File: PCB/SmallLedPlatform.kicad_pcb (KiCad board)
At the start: 4 copper layers, 44.7 x 36.1 mm, 47 parts, among them J101 USB_C_Receptacle, J102 Conn_02x05_Odd_Even, J103 Conn_01x03_Male, J104 Conn_01x03_Male, Q101 AO3400A, U101 STM32G0B1CBTx, U102 USBLC6-2P6, U103 TCPP01-M12, U201 TPS5430DDA, U202 XC6206PxxxMR

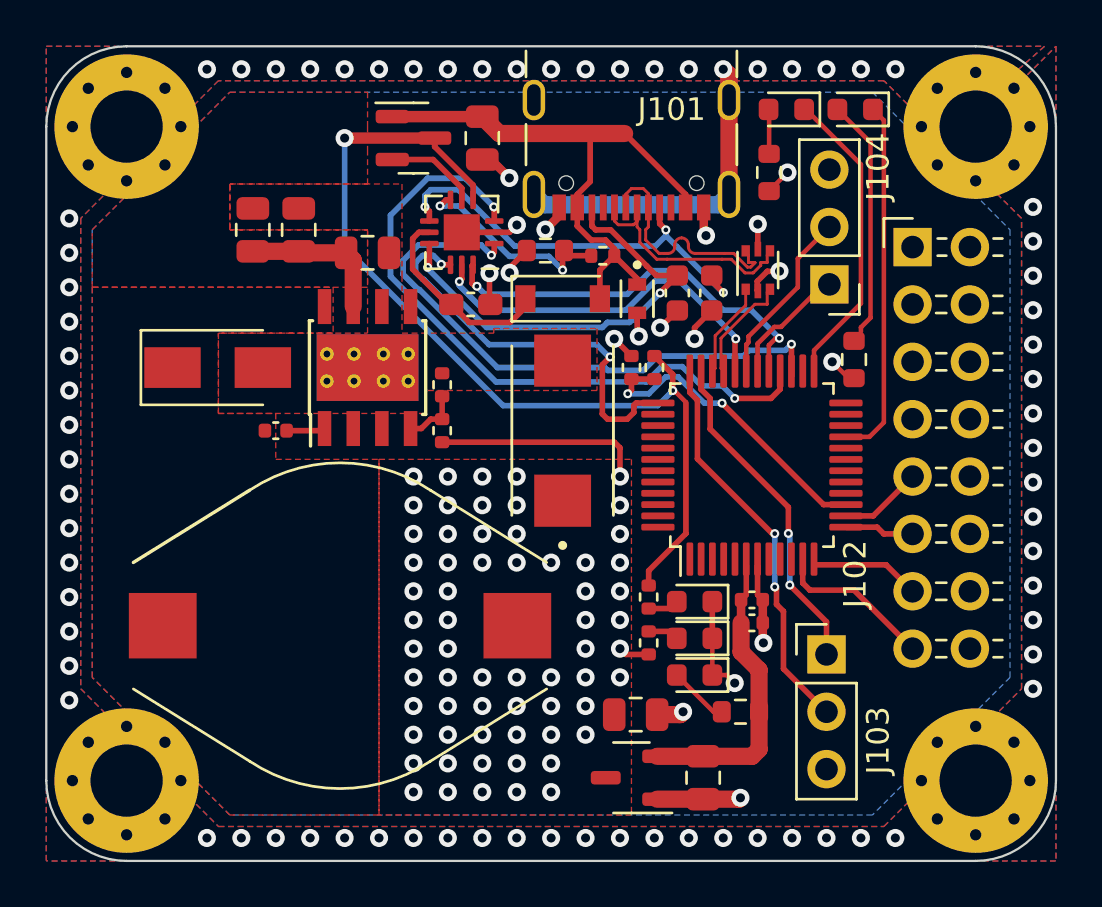
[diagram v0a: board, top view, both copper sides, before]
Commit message: Add a new DC/DC solution to the schematic
Components has been added to layout, but not properly done
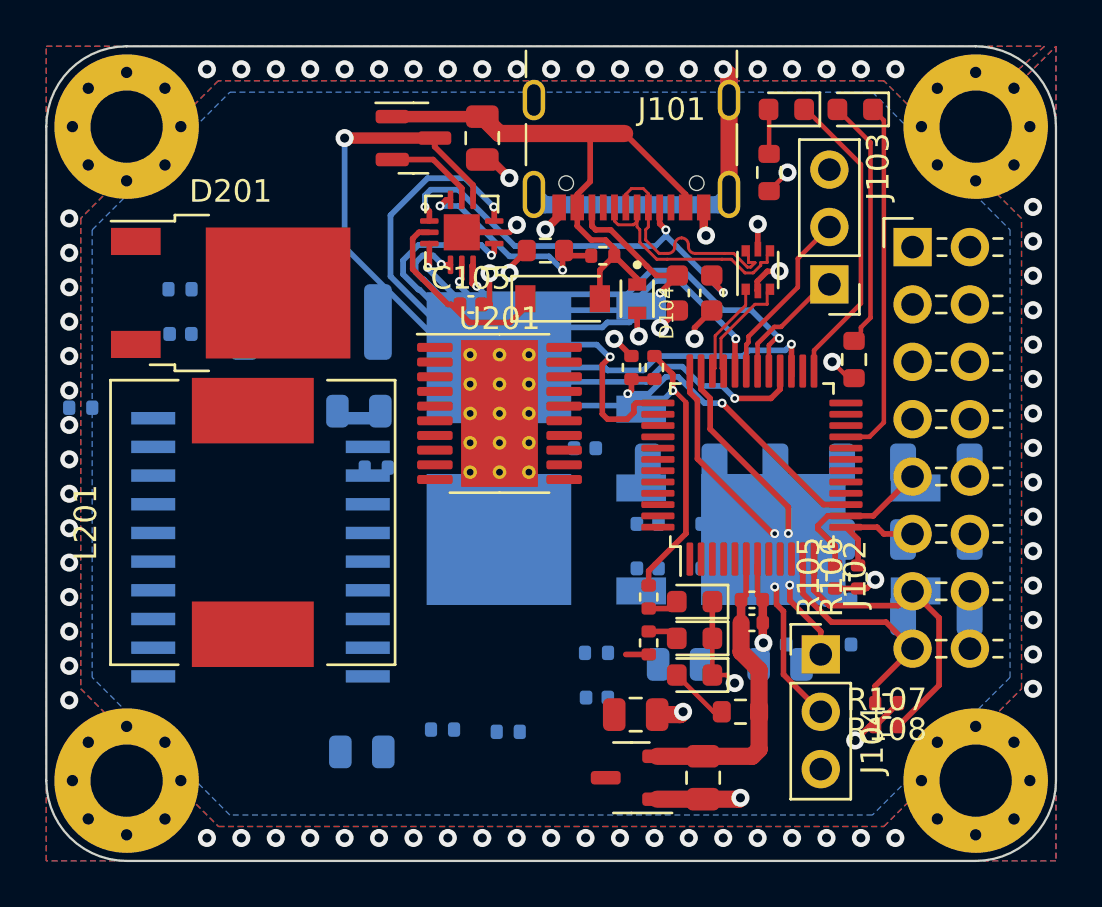
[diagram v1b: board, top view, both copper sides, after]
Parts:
- added C103: 2,2uF/50V, Capacitor_SMD:C_0805_2012Metric, B.Cu at (124.2, 110.0)
- added C206: 22nF/50V, Capacitor_SMD:C_0402_1005Metric, B.Cu at (142.5, 105.2)
- added C207: 120pF/50V, Capacitor_SMD:C_0402_1005Metric, B.Cu at (134.1, 96.5)
- added C208: 120pF/50V, Capacitor_SMD:C_0402_1005Metric, B.Cu at (139.7, 99.9)
- added C209: 10nF/50V, Capacitor_SMD:C_0402_1005Metric, B.Cu at (145.4, 105.2)
- added C210: 1uF/25V, Capacitor_SMD:C_0402_1005Metric, B.Cu at (136.9, 101.9)
- added C211: 100uF/10V, Capacitor_SMD:C_1206_3216Metric, B.Cu at (149.6, 100.6)
- added C212: 100uF/10V, Capacitor_SMD:C_1206_3216Metric, B.Cu at (144.0, 100.6)
- added C213: 100uF/10V, Capacitor_SMD:C_1206_3216Metric, B.Cu at (138.3, 97.2)
- added C214: 100uF/10V, Capacitor_SMD:C_1206_3216Metric, B.Cu at (149.6, 103.9)
- added C215: 470nF/10V, Capacitor_SMD:C_0402_1005Metric, B.Cu at (136.9, 99.9)
- added C216: 470nF/6.3V, Capacitor_SMD:C_0402_1005Metric, B.Cu at (139.7, 101.9)
- added C217: 100uF/10V, Capacitor_SMD:C_1206_3216Metric, B.Cu at (144.0, 97.2)
- added C218: 100uF/10V, Capacitor_SMD:C_1206_3216Metric, B.Cu at (149.6, 97.2)
- added D202: MBR20150CD, Package_TO_SOT_SMD:TO-252-2, B.Cu at (132.4, 92.5)
- added Q201: IRFR7440TRPBF, Package_TO_SOT_SMD:TO-252-2, B.Cu at (132.4, 100.6)
- added Q202: IRFR7440TRPBF, Package_TO_SOT_SMD:TO-252-2, B.Cu at (144.5, 100.6)
- added R105: 470R, Resistor_SMD:R_0402_1005Metric, F.Cu at (145.2, 102.2)
- added R106: 470R, Resistor_SMD:R_0402_1005Metric, F.Cu at (146.2, 102.2)
- added R107: 470R, Resistor_SMD:R_0402_1005Metric, F.Cu at (147.4, 108.8)
- added R108: 470R, Resistor_SMD:R_0402_1005Metric, F.Cu at (147.4, 107.8)
- added R203: 10k, Resistor_SMD:R_0402_1005Metric, B.Cu at (134.6, 105.6)
- added R204: 10k, Resistor_SMD:R_0402_1005Metric, B.Cu at (127.8, 109.0)
- added R205: 3.24k, Resistor_SMD:R_0402_1005Metric, B.Cu at (116.2, 89.5)
- added R206: 18k, Resistor_SMD:R_0402_1005Metric, B.Cu at (124.8, 97.4)
- added R207: 1k, Resistor_SMD:R_0402_1005Metric, B.Cu at (130.7, 109.1)
- added R208: 1k, Resistor_SMD:R_0402_1005Metric, B.Cu at (111.8, 94.7)
- added U202: BTS724G, Package_SO:Infineon_PG-DSO-20-32, B.Cu at (119.7, 100.9)
- C105: renamed from C104; footprint Capacitor_SMD:C_0603_1608Metric_Pad1.08x0.95mm_HandSolder -> Capacitor_SMD:C_0402_1005Metric
- C201: value 10nF/50V -> 10uF/50V; footprint Capacitor_SMD:C_0402_1005Metric -> Capacitor_SMD:C_0805_2012Metric; moved to B.Cu
- C202, C203: value 2,2uF/50V -> 10uF/50V; moved to B.Cu
- C204: value 2,2uF/50V -> 100nF/50V; footprint Capacitor_SMD:C_0805_2012Metric -> Capacitor_SMD:C_0402_1005Metric; moved to B.Cu
- C205: value 330uF/6.3V -> 100n/16V; footprint Skrooter_footprints:CAPPM7343X310N -> Capacitor_SMD:C_0402_1005Metric; moved to B.Cu
- D201: value SS54 -> MBR20150CD; footprint Diode_SMD:D_SMA -> Package_TO_SOT_SMD:TO-252-2
- L201: value SMSD1306-150MT -> 1.8uH; footprint Inductor_SMD:L_Bourns_SDR1806 -> Inductor_SMD:L_12x12mm_H8mm
- R201: value 10k -> 1M; moved to B.Cu
- R202: value 3.24k -> 7mR; footprint Resistor_SMD:R_0402_1005Metric -> Resistor_SMD:R_2512_6332Metric; moved to B.Cu
- U201: value TPS5430DDA -> LM25118; footprint Package_SO:TI_SO-PowerPAD-8_ThermalVias -> Package_SO:HTSSOP-20-1EP_4.4x6.5mm_P0.65mm_EP3.4x6.5mm_Mask2.75x3.43mm_ThermalVias
- moved C202 27.0 mm to (138.3, 106.1), turned to 180 degrees
- moved C201 24.6 mm to (142.7, 106.1)
- moved C204 24.6 mm to (134.6, 107.6), turned to 180 degrees
- moved R201 19.1 mm to (145.4, 103.2), turned to 180 degrees
- moved C205 17.5 mm to (116.2, 91.5), turned to 180 degrees
- moved C203 7.02 mm to (124.1, 94.9), turned to 180 degrees
- moved R202 6.44 mm to (122.0, 90.9), turned to 180 degrees
- moved U201 6.19 mm to (130.3, 95.0), turned to 0 degrees
- moved L201 5.98 mm to (119.4, 99.8), turned to 90 degrees
- moved D201 3.35 mm to (118.4, 89.7)
- moved J104 0.25 mm to (144.5, 105.7)
- renumbered C103 to C104, C105 to C106, C106 to C107, C206 to C219, C207 to C220, D202 to D203, D203 to D204, D204 to D205, J104 to J103, J103 to J104, R104 to R101, R106 to R102, R101 to R103, R102 to R104, R103 to R109, R105 to R110, R203 to R209, R204 to R210, R205 to R211, U202 to U203
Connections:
- C201 pad 1: /Power/BOOT -> /Power/VIN
- C201 pad 2: /Power/PH -> GND
- C202 pad 1: VBUS -> /Power/VIN
- C203 pad 1: VBUS -> /Power/VIN
- C204 pad 1: VBUS -> /Power/VIN
- C205 pad 1: +5V -> Net-(U201-Pad18)
- C205 pad 2: GND -> Net-(L201-Pad1)
- D201 pad 1: /Power/PH -> Net-(L201-Pad2)
- D201 pad 2: GND -> Net-(L201-Pad2)
- L201 pad 1: /Power/PH -> Net-(L201-Pad1)
- L201 pad 2: +5V -> Net-(L201-Pad2)
- R201 pad 1: +5V -> /Power/VIN
- R201 pad 2: /Power/DCDC_VSENSE -> Net-(U201-Pad4)
- R202 pad 1: /Power/DCDC_VSENSE -> Net-(U201-Pad12)
- R202 pad 2: GND -> Net-(U201-Pad13)
- U201 pad 1: /Power/BOOT -> /Power/VIN
- U201 pad 3: unconnected-(U201-Pad3) -> Net-(R204-Pad1)
- U201 pad 4: /Power/DCDC_VSENSE -> Net-(U201-Pad4)
- U201 pad 5: unconnected-(U201-Pad5) -> Net-(C207-Pad1)
- U201 pad 7: VBUS -> Net-(C206-Pad1)
- U201 pad 8: /Power/PH -> Net-(U201-Pad8)
- U201 pad 9: GND -> Net-(U201-Pad9)
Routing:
- net /LEDOUT_2: track 4.85 -> 13.5 mm
- net VBUS: track 48.1 -> 41.4 mm
- net +5V: track 14.2 -> 9.08 mm, vias 66 -> 5
- net /LEDOUT_3: track 6.87 -> 10.5 mm
- net /LEDOUT_0: track 3.67 -> 7.16 mm
- net /Power/DCDC_VSENSE: track 2.58 -> 0.00 mm
- net /LEDOUT_1: track 3.07 -> 4.99 mm
- net /Power/BOOT: track 1.72 -> 0.00 mm
- removed copper zone on F.Cu, net +5V
- removed copper zone on F.Cu, net /Power/PH
- removed copper zone on F.Cu, net GND
- removed copper zone on F.Cu, net VBUS

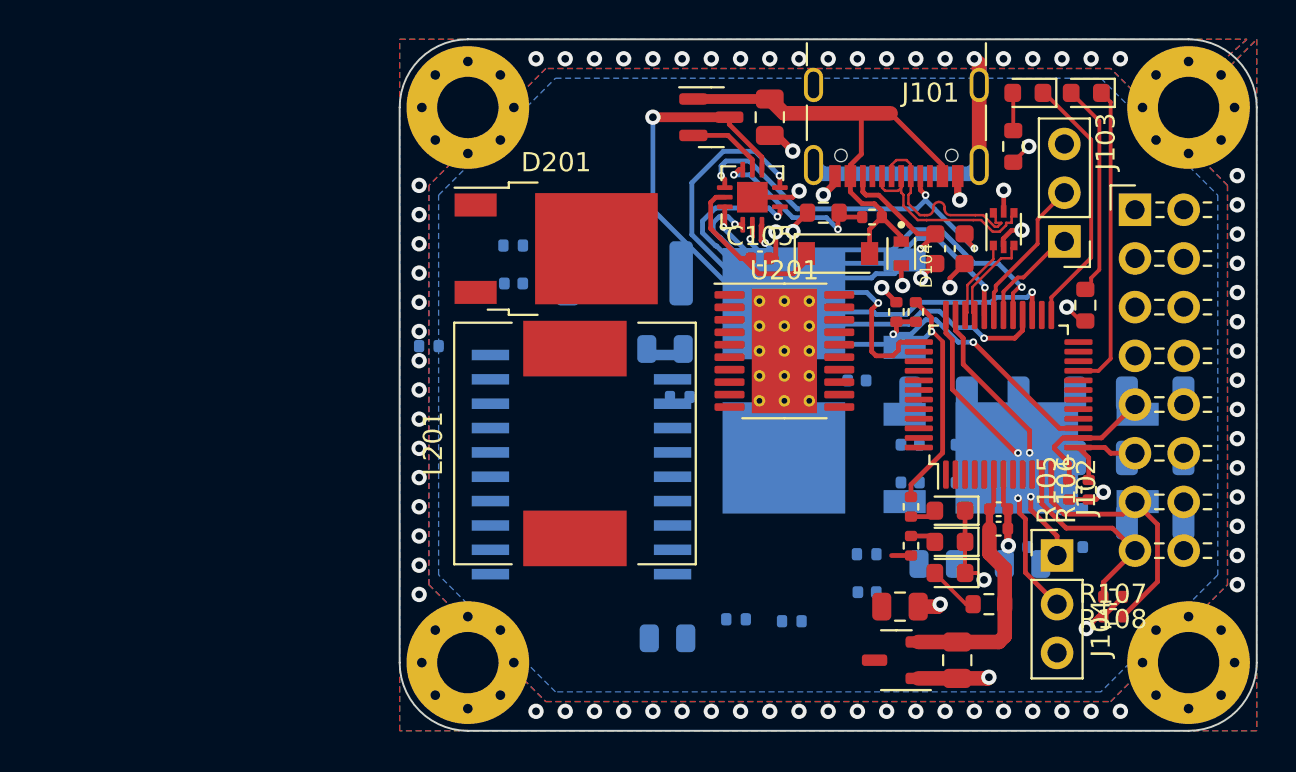
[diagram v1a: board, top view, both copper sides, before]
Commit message: reroute pretty much everything
Routing is done for new DC/DC!
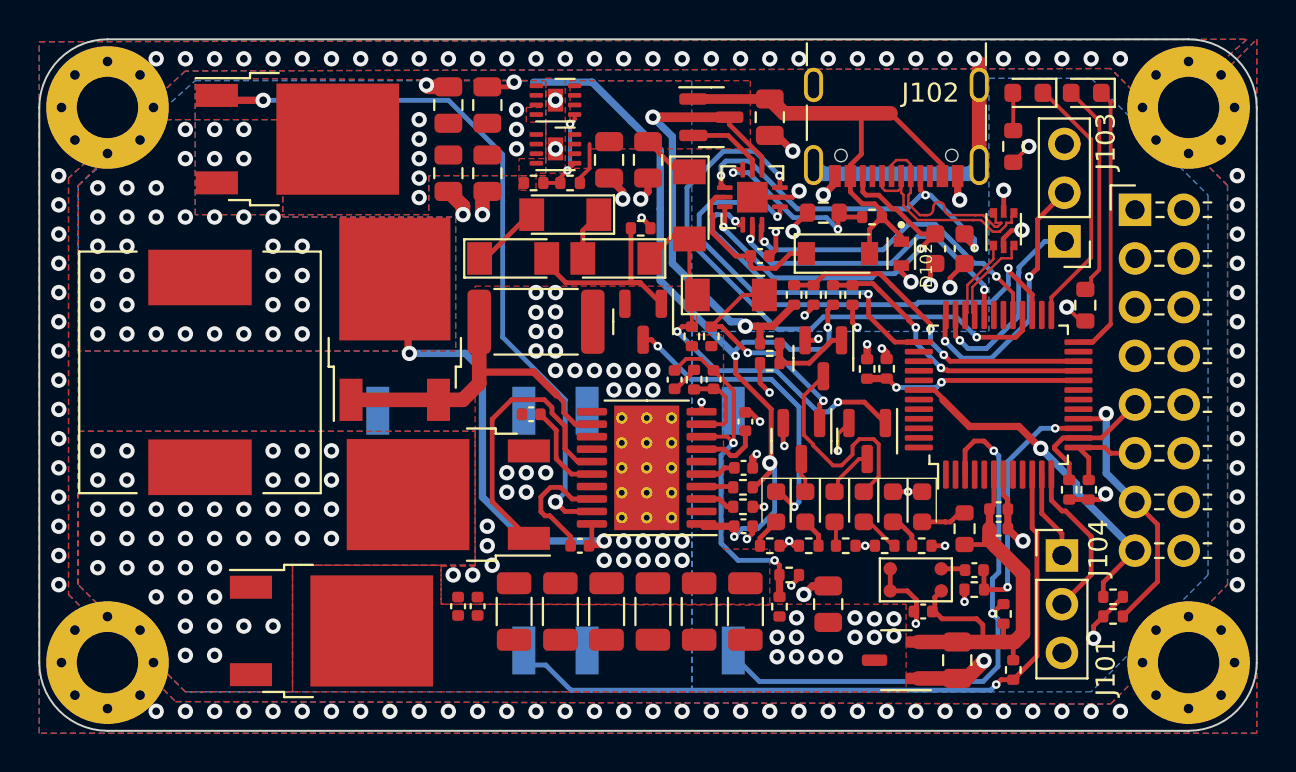
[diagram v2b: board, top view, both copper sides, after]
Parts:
- removed D203, D204, D205: Yellow, LED_SMD:LED_0603_1608Metric
- removed the R101 at (137.2, 93.0)
- removed the R102 at (136.1, 93.0)
- removed the R207 at (130.7, 109.1)
- removed the R210 at (136.9, 105.2)
- removed the U202 at (119.7, 100.9)
- added C217: 10uF/50V, Capacitor_SMD:C_0805_2012Metric, F.Cu at (121.2, 85.0)
- added C218: 10uF/50V, Capacitor_SMD:C_0805_2012Metric, F.Cu at (114.8, 85.7)
- added C401: 100nF/50V, Capacitor_SMD:C_0402_1005Metric, F.Cu at (137.5, 108.6)
- added C402: 100nF/50V, Capacitor_SMD:C_0402_1005Metric, F.Cu at (140.2, 106.4)
- added D301: 5.6V, Diode_SMD:D_MiniMELF, F.Cu at (125.3, 87.4)
- added D302: 5.6V, Diode_SMD:D_MiniMELF, F.Cu at (127.5, 92.1)
- added D303: 3v3V, Diode_SMD:D_MiniMELF, F.Cu at (121.5, 90.2)
- added D304: Yellow, Skrooter_footprints:LED_0603_1608Metric_smaller_silk, F.Cu at (134.4, 103.1)
- added D305: Yellow, Skrooter_footprints:LED_0603_1608Metric_smaller_silk, F.Cu at (132.9, 103.1)
- added D306: Yellow, Skrooter_footprints:LED_0603_1608Metric_smaller_silk, F.Cu at (131.4, 103.1)
- added D307: Yellow, Skrooter_footprints:LED_0603_1608Metric_smaller_silk, F.Cu at (129.9, 103.1)
- added D308: Yellow, Skrooter_footprints:LED_0603_1608Metric_smaller_silk, F.Cu at (136.0, 103.1)
- added D309: Yellow, Skrooter_footprints:LED_0603_1608Metric_smaller_silk, F.Cu at (137.5, 103.1)
- added D310: 3v3V, Diode_SMD:D_MiniMELF, F.Cu at (118.9, 87.9)
- added D311: 3v3V, Diode_SMD:D_MiniMELF, F.Cu at (116.2, 90.2)
- added Q301: 2N7002, Package_TO_SOT_SMD:SOT-23, F.Cu at (132.3, 95.4)
- added Q302: 2N7002, Package_TO_SOT_SMD:SOT-23, F.Cu at (134.6, 99.7)
- added Q303: 2N7002, Package_TO_SOT_SMD:SOT-23, F.Cu at (131.2, 99.7)
- added Q304: 2N7002, Package_TO_SOT_SMD:SOT-23, F.Cu at (122.9, 93.5)
- added R106: 10k, Resistor_SMD:R_0402_1005Metric, F.Cu at (130.8, 92.1)
- added R108: 1k5, Resistor_SMD:R_0402_1005Metric, F.Cu at (131.8, 92.1)
- added R205: 10k, Resistor_SMD:R_0402_1005Metric, F.Cu at (132.8, 92.1)
- added R206: 1k, Resistor_SMD:R_0402_1005Metric, F.Cu at (134.6, 95.9)
- added R212: 10k, Resistor_SMD:R_0402_1005Metric, F.Cu at (117.2, 86.2)
- added R301: 68k, Resistor_SMD:R_0402_1005Metric, F.Cu at (129.5, 94.6)
- added R302: 150R, Resistor_SMD:R_0402_1005Metric, F.Cu at (135.5, 105.2)
- added R303: 150R, Resistor_SMD:R_0402_1005Metric, F.Cu at (133.5, 105.2)
- added R304: 150R, Resistor_SMD:R_0402_1005Metric, F.Cu at (131.6, 105.2)
- added R305: 150R, Resistor_SMD:R_0402_1005Metric, F.Cu at (129.5, 105.2)
- added R306: 150R, Resistor_SMD:R_0402_1005Metric, F.Cu at (137.5, 105.2)
- added R307: 68R, Resistor_SMD:R_0603_1608Metric, F.Cu at (139.7, 104.3)
- added R308: 100k, Resistor_SMD:R_0402_1005Metric, F.Cu at (129.5, 95.6)
- added R309: 100k, Resistor_SMD:R_0402_1005Metric, F.Cu at (125.5, 94.2)
- added R310: 100k, Resistor_SMD:R_0402_1005Metric, F.Cu at (126.5, 94.2)
- added R311: 100k, Resistor_SMD:R_0402_1005Metric, F.Cu at (122.8, 88.6)
- added R401: 100k, Resistor_SMD:R_0402_1005Metric, F.Cu at (140.2, 107.4)
- added R402: 10k, Resistor_SMD:R_0402_1005Metric, F.Cu at (142.2, 111.6)
- added R403: 10k, Resistor_SMD:R_0402_1005Metric, F.Cu at (141.7, 108.7)
- added SW401: SW_MEC_5E, Button_Switch_SMD:SW_MEC_5GSH9, B.Cu at (112.9, 104.4)
- added SW402: SW_MEC_5E, Button_Switch_SMD:SW_MEC_5GSH9, B.Cu at (123.8, 104.4)
- added U203: WS3222D, Package_DFN_QFN:WDFN-8-1EP_2x2mm_P0.5mm_EP0.8x1.2mm, F.Cu at (118.4, 81.9)
- added U204: WS3222D, Package_DFN_QFN:WDFN-8-1EP_2x2mm_P0.5mm_EP0.8x1.2mm, F.Cu at (118.4, 84.5)
- added U401: AP3722AT, Skrooter_footprints:AP3722AT, F.Cu at (138.5, 107.5)
- C103, C201, C202, C203, C204, C205, D202, Q201, Q202, R201, R202, R203, R204: moved to F.Cu
- C208: renamed from C206; moved to F.Cu
- C209: renamed from C207; moved to F.Cu
- C210: renamed from C208; moved to F.Cu
- C211: renamed from C209; moved to F.Cu
- C212: renamed from C210; moved to F.Cu
- C213: renamed from C211; moved to F.Cu
- C214: renamed from C212; moved to F.Cu
- C215: renamed from C213; moved to F.Cu
- C216: renamed from C214; moved to F.Cu
- C219: renamed from C215; moved to F.Cu
- C220: renamed from C216; moved to F.Cu
- C221: renamed from C217; moved to F.Cu
- C222: renamed from C218; moved to F.Cu
- R207: renamed from R205; moved to F.Cu
- R208: value 1k -> 1k5; moved to F.Cu
- R209: value 1k -> 1k5
- R210: renamed from R206; moved to F.Cu
- R211: value 65R -> 18k; footprint Resistor_SMD:R_0603_1608Metric -> Resistor_SMD:R_0402_1005Metric
- moved C201 36.2 mm to (112.8, 85.7), turned to -90 degrees
- moved C213 34.4 mm to (116.2, 108.6), turned to 90 degrees
- moved C202 33.5 mm to (114.8, 82.2), turned to 90 degrees
- moved Q201 32.1 mm to (104.9, 83.9), turned to 0 degrees
- moved Q202 31.8 mm to (112.8, 102.5)
- moved R211 31.0 mm to (119.1, 86.2)
- moved C220 27.2 mm to (113.3, 108.3), turned to 90 degrees
- moved C216 26.6 mm to (123.4, 108.6), turned to 90 degrees
- moved C214 26.6 mm to (118.6, 108.6), turned to 90 degrees
- moved C103 25.0 mm to (123.2, 85.0), turned to -90 degrees
- moved C222 24.2 mm to (128.3, 108.6), turned to 90 degrees
- moved C219 24.1 mm to (114.3, 108.3), turned to 90 degrees
- moved D201 23.1 mm to (106.7, 109.6)
- moved C211 22.6 mm to (124.6, 96.5), turned to -90 degrees
- moved R207 22.4 mm to (130.6, 106.7), turned to 0 degrees
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- renumbered C219 to C206, C220 to C207, D103 to D101, D104 to D102, D101 to D401, D102 to D402, J104 to J101, J101 to J102, J102 to J104, R105 to R101, R106 to R102, R107 to R103, R108 to R104, R109 to R105, R110 to R107, R103 to R404, R104 to R405, U203 to U202
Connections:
- net Net-(C206-Pad1) renamed /Power/SS
- net Net-(C207-Pad1) renamed /Power/RAMP
- net Net-(C209-Pad2) renamed /Power/COMP_filter
- net Net-(R204-Pad1) renamed /Power/RT
- net Net-(U201-Pad15) renamed /Power/LO
- net Net-(U201-Pad16) renamed /Power/VCC
- net Net-(U201-Pad18) renamed /Power/HB
- net Net-(U201-Pad19) renamed /Power/HO
- net Net-(U201-Pad4) renamed /Power/EN
- net Net-(U201-Pad8) renamed /Power/FB
- net Net-(U201-Pad9) renamed /Power/COMP
- C103 pad 1: VBUS -> IN
- C205 pad 2: Net-(L201-Pad1) -> /Power/HS
- D201 pad 1: Net-(L201-Pad2) -> /Power/dcdc_coil
- D201 pad 2: Net-(L201-Pad2) -> +5V
- D201 pad 3: +5V -> /Power/dcdc_coil
- D202 pad 1: Net-(U201-Pad12) -> /Power/CS
- D202 pad 2: Net-(U201-Pad12) -> /Power/HS
- D202 pad 3: Net-(L201-Pad1) -> /Power/CS
- J101 pad 1: /SWD_SWDIO -> /DEBUG_UART_TX
- J101 pad 2: /SWD_SWCLK -> /DEBUG_UART_RX
- J103 pad 1: /DEBUG_UART_TX -> /SWD_SWDIO
- J103 pad 2: /DEBUG_UART_RX -> /SWD_SWCLK
- L201 pad 1: Net-(L201-Pad1) -> /Power/HS
- L201 pad 2: Net-(L201-Pad2) -> /Power/dcdc_coil
- Q101 pad 3: VBUS -> IN
- Q201 pad 3: Net-(L201-Pad1) -> /Power/HS
- Q202 pad 2: Net-(L201-Pad2) -> /Power/dcdc_coil
- R202 pad 1: Net-(U201-Pad12) -> /Power/CS
- R202 pad 2: Net-(U201-Pad13) -> GND
- R208 pad 1: +3V3 -> /Power/VIN_SENSE
- R208 pad 2: /Power/DIAG_HS_SWITCH2 -> GND
- R209 pad 1: VBUS -> /Power/5V_Sense
- R209 pad 2: Net-(D203-Pad2) -> GND
- R211 pad 1: +3V3 -> IN
- R211 pad 2: Net-(D205-Pad2) -> /Power/OVLO
- U101 pad 10: unconnected-(U101-Pad10) -> /MCU_SW1
- U101 pad 11: /LEDOUT_3 -> /DEBUG_UART_TX
- U101 pad 12: /LEDOUT_2 -> /DEBUG_UART_RX
- U101 pad 15: /VBUS_SENSE -> /MIC_MCU
- U101 pad 16: unconnected-(U101-Pad16) -> /LEDOUT_2
- U101 pad 20: unconnected-(U101-Pad20) -> /Power/5V_Sense
- U101 pad 21: /LED2 -> /Power/VIN_SENSE
- U101 pad 22: unconnected-(U101-Pad22) -> /VBUS_SENSE
- U101 pad 24: unconnected-(U101-Pad24) -> /LED2
- U101 pad 3: unconnected-(U101-Pad3) -> /MCU_SW2
- U101 pad 30: /DEBUG_UART_TX -> unconnected-(U101-Pad30)
- U101 pad 31: /DEBUG_UART_RX -> unconnected-(U101-Pad31)
- U101 pad 42: unconnected-(U101-Pad42) -> /LEDOUT_3
- U103 pad 4: VBUS -> IN
- U201 pad 12: Net-(U201-Pad12) -> /Power/CS
- U201 pad 13: Net-(U201-Pad13) -> GND
- U201 pad 20: Net-(L201-Pad1) -> /Power/HS
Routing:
- net /Power/VIN: track 0.00 -> 43.8 mm, vias 0 -> 12
- net VBUS: track 41.4 -> 0.00 mm, vias 2 -> 0
- net /Power/HO: track 0.00 -> 38.0 mm, vias 0 -> 2
- net /MCU_SW1: track 0.00 -> 37.8 mm, vias 0 -> 1
- net /MCU_SW2: track 0.00 -> 30.3 mm, vias 0 -> 2
- net IN: track 0.00 -> 29.6 mm, vias 0 -> 2
- net /Power/HS: track 0.00 -> 23.8 mm, vias 0 -> 38
- net GND: track 28.6 -> 50.8 mm, vias 15 -> 73
- net /Power/Power LEDS/9v_gate: track 0.00 -> 21.5 mm, vias 0 -> 2
- net /Power/FB: track 0.00 -> 18.9 mm, vias 0 -> 2
- net /Power/CS: track 0.00 -> 17.6 mm
- net /Power/Power LEDS/20v_led_k: track 0.00 -> 16.2 mm, vias 0 -> 2
- net /Power/VIN_SENSE: track 0.00 -> 15.2 mm, vias 0 -> 2
- net /Power/LO: track 0.00 -> 14.8 mm
- net /MIC_MCU: track 0.00 -> 13.3 mm, vias 0 -> 2
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- added copper zone on F.Cu, net +5V
- added copper zone on B.Cu, net /Power/HS
- added copper zone on F.Cu, net /Power/HS
- added copper zone on B.Cu, net /Power/VIN
- added copper zone on F.Cu, net /Power/VIN
- added copper zone on B.Cu, net /Power/dcdc_coil
- added copper zone on F.Cu, net /Power/dcdc_coil
- added copper zone on B.Cu, net GND
- added copper zone on F.Cu, net GND
- added copper zone on F.Cu, net IN
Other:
- board size 44.7 x 36.1 mm -> 63.5 x 36.1 mm
